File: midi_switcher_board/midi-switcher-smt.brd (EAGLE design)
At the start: 104.1 x 41.9 mm, 79 parts, among them IC1 6N138, IC2 PIC16F1825SO14, IC3 LD1086, Q1 MJD122GDPAK, Q2 MJD122GDPAK, Q3 MJD122GDPAK, Q4 MJD122GDPAK, Q5 MJD122GDPAK, Q6 MJD122GDPAK, Q7 MJD122GDPAK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

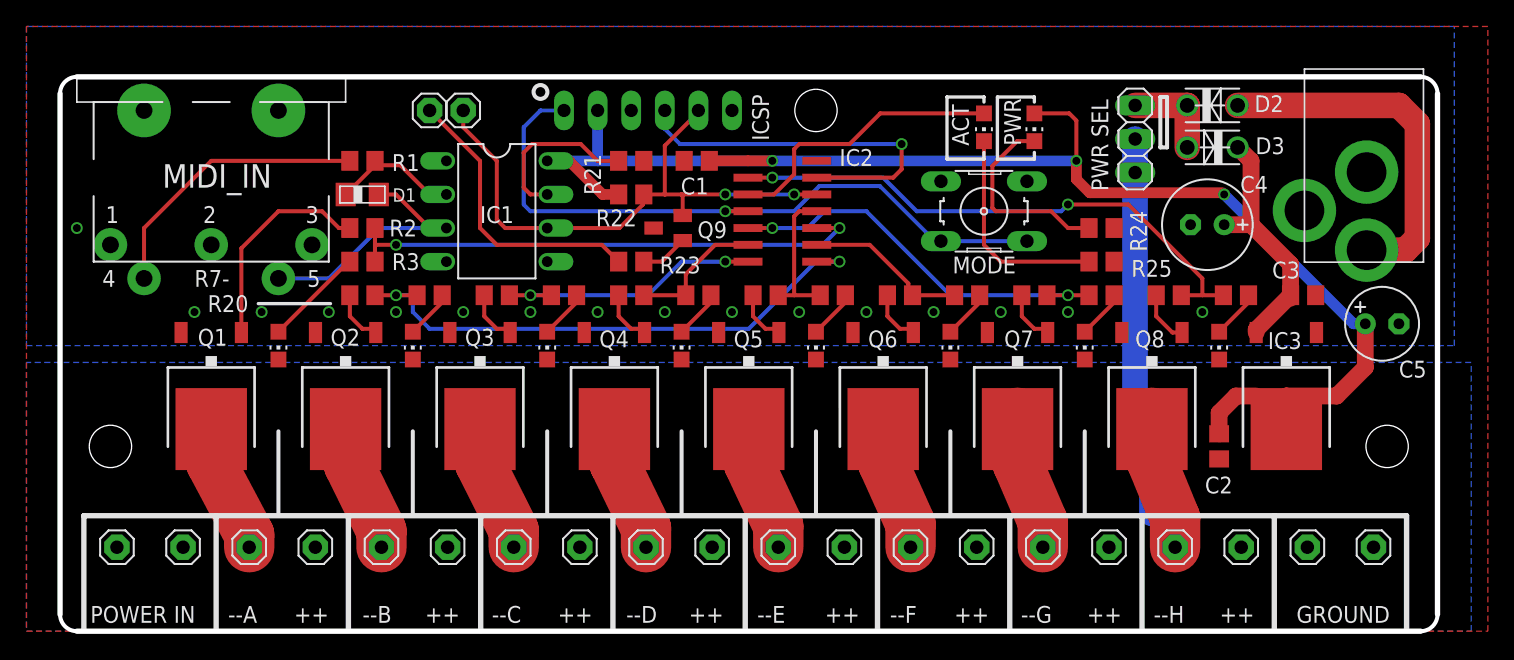
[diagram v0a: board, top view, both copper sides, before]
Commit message: segment large pads/tidy up
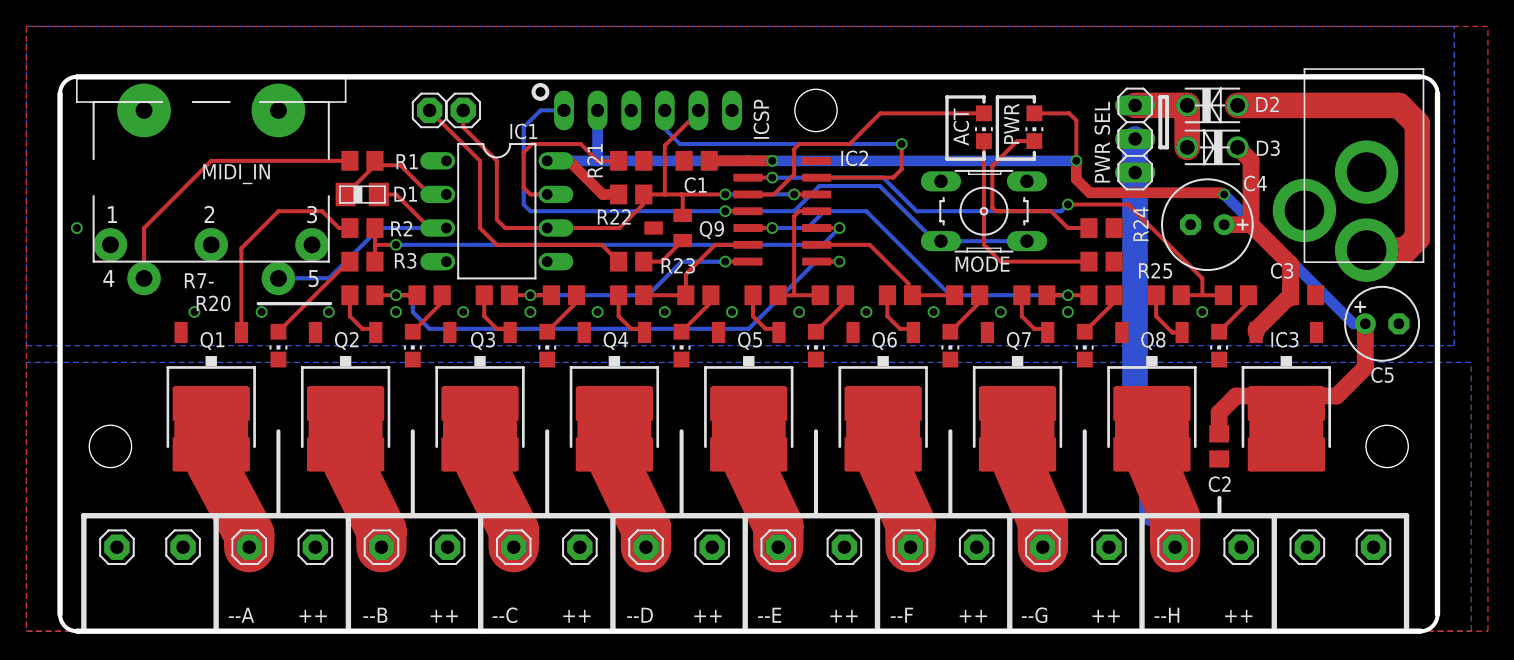
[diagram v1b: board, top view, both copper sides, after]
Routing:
- net +5V: track 112.1 -> 114.9 mm
- net N$42: track 9.61 -> 11.5 mm
- net N$26: track 10.6 -> 9.20 mm
- net N$25: track 10.5 -> 9.15 mm
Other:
- board text added: "POWER"
- board text removed: "POWER IN"
